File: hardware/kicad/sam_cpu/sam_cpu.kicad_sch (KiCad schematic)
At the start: 0 parts

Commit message: Redraw the schematic with wires (draft 0.2)
Every connection is now a wire, and each connector sits on the page of the
parts that drive or read it (Pi header with the RP2354B, J6/J12 with their
comparators and 74HC165, J1 with the 74HC595, J2/J3/J13 with their filters).
Signals between pages use global labels with page references. The Pi page is
merged into the MCU page; the Pi 4 sits on the 40-pin header J21.

ERC: 0 errors, 1 warning. Netlist check: 1266 pins, 299 nets, no differences.

Co-Authored-By: Claude Opus 5.5 (1M context) <noreply@anthropic.com>
Claude-Session: https://claude.ai/code/session_019DLTv1F2PjepjxqiUcAMKV
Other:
- sheet MCU renamed MCU and Pi
- removed sheet Dedicated switches
- removed sheet Raspberry Pi
- removed sheet Switch returns
- removed sheet Switch scan
- added sheet Dedicated switches 1-16 (sw_dedicated_1.kicad_sch)
- added sheet Dedicated switches 17-24 (sw_dedicated_2.kicad_sch)
- added sheet Switch columns (sw_columns.kicad_sch)
- added sheet Switch rows 1-8 (sw_rows_1.kicad_sch)
- added sheet Switch rows 9-16 (sw_rows_9.kicad_sch)
- sheet Audio ports: added none; removed I2S_BCK, I2S_DIN, I2S_LRCK
- sheet Display and GI ports: added none; removed DMD_COLLATCH_A, DMD_COLLATCH_B, DMD_DE, DMD_PIXCLK, DMD_ROWCLK, DMD_ROWDATA, DMD_SDATA, GI_PWM, GI_SPARE
- sheet IO bus ports: added none; removed BUS_A0, BUS_A1, BUS_A2, BUS_A3, BUS_D0, BUS_D1, BUS_D2, BUS_D3, BUS_D4, BUS_D5, BUS_D6, BUS_D7, BUS_DIR, BUS_IOSTB, BUS_OE_N, NBRESET_DRV
- sheet MCU and Pi ports: added none; removed BOOTSEL, BUS_A0, BUS_A1, BUS_A2, BUS_A3, BUS_D0, BUS_D1, BUS_D2, BUS_D3, BUS_D4, BUS_D5, BUS_D6, BUS_D7, BUS_DIR, BUS_IOSTB, BUS_OE_N, DMD_COLLATCH_A, DMD_COLLATCH_B, DMD_DE, DMD_PIXCLK, DMD_ROWCLK, DMD_ROWDATA, DMD_SDATA, FRAME_CS_N, FRAME_MOSI, FRAME_SCK, GI_PWM, GI_SPARE, MEM_PROTECT, MR_N, NBRESET_DRV, RP_IRQ_N, RP_UART_RX, RP_UART_TX, STB_DATA, STB_LATCH, SWCLK, SWDIO, SW_CLK, SW_DATA, SW_LOAD_N, VMON_12V, VMON_5V
- sheet Power ports: added none; removed VMON_12V, VMON_5V
- note added: "Audio: Pi I2S -> PCM5102A -> 2 x TDA2030A on +-12 V -> J10"
- note added: "Dedicated switches D1-D16 (J2, J3) and coin door memory protect"
- note added: "Dedicated switches D17-D24 (J13) and DIP switches"
- note added: "J5 original DMD driver and J18 GI dimmer header"
- note added: "J9: bus to the IO power driver board (IO board J1)"
- note added: "Power: +5 V mux (external / J11), 3.3 V, 4.5 V, supply monitors"
- note added: "RP2354B SAM IO controller and Raspberry Pi 4 header"
- note added: "SAM CPU replacement board, draft 0.2, drawn from docs/ARCHITECTURE.md. Licence: CERN-OHL-S v2. A Raspberry Pi 4 on the 40-pin header J21 runs PinMAME + ppuc (HDMI stays on the Pi). The RP2354B drives the original IO power driver board on J9 and scans the switches. Connector names and pinouts follow the original CPU/Sound board 520-5246-00. Each connector sits on the same page as the circuit that 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"
- note added: "Switch matrix columns: 74HC595, strobe drivers, J1"
- note added: "Switch matrix returns 1-8: J6, LM339 front end, 74HC165"
- note added: "Switch matrix returns 9-16: J12, LM339 front end, 74HC165"
- note removed: "SAM CPU replacement board, draft 0.1, drawn from docs/ARCHITECTURE.md. A Raspberry Pi 4 / CM4 runs PinMAME + ppuc. The RP2354B drives the original IO power driver board on J9 and scans the switches. Connector names and pinouts follow the original CPU/Sound board 520-5246-00. Licence: CERN-OHL-S v2."

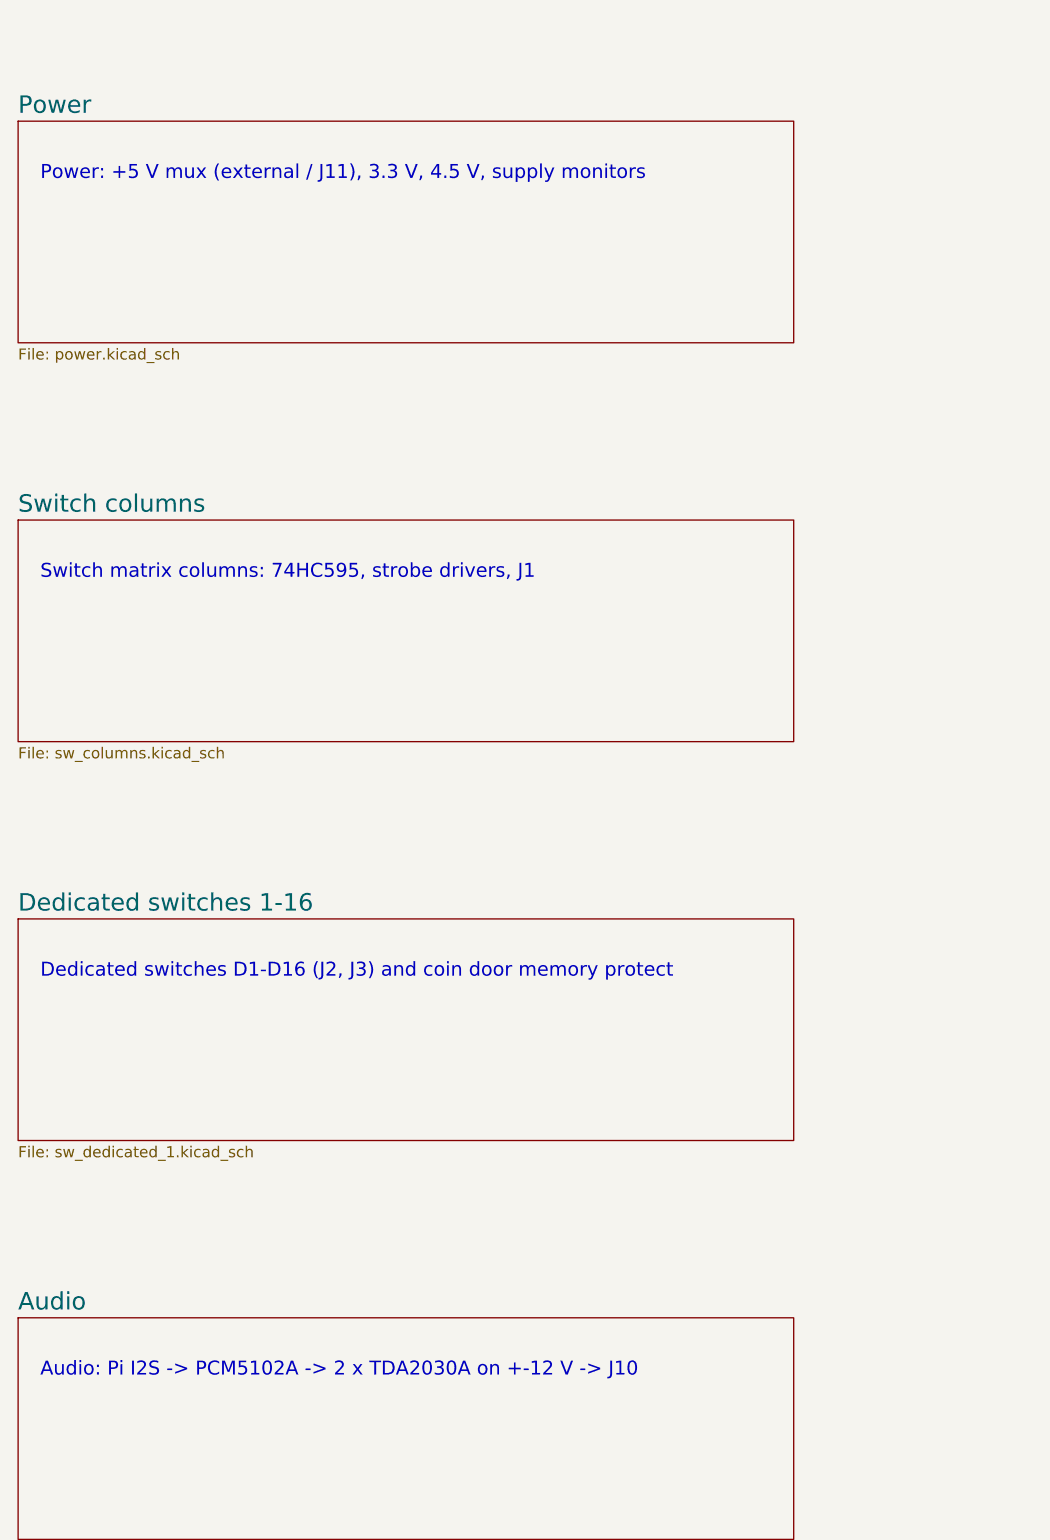
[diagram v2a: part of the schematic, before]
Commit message: Audio on external 12 V with TDA7297 stereo + subwoofer amps, NCP1117, guide regulator layout
- Remove the +-12 V input from J11; J23 external +12 V with polyfuse and TVS
- Replace the two TDA2030A with a TDA7297 bridge amp for left/right (J10, J22)
  and a second TDA7297 for the subwoofer (J24), fed by an (L+R)/2 110 Hz
  Sallen-Key low-pass (OPA1678); shared standby and RP2354B-controlled mute
- AMS1117 -> NCP1117-3.3 (ceramic-stable, as in the RP2350 guide), 10 uF 1206
- L1 and crystal part numbers from the RP2350 hardware guide
- Place the core regulator parts by hand following the Pico 2 layout; amps in a
  row with a heatsink keep-out; J23/J22/J24 on the right edge

Co-Authored-By: Claude Opus 5.5 (1M context) <noreply@anthropic.com>
Claude-Session: https://claude.ai/code/session_01ExuDVoDDDHhVWjb8EwVzYb
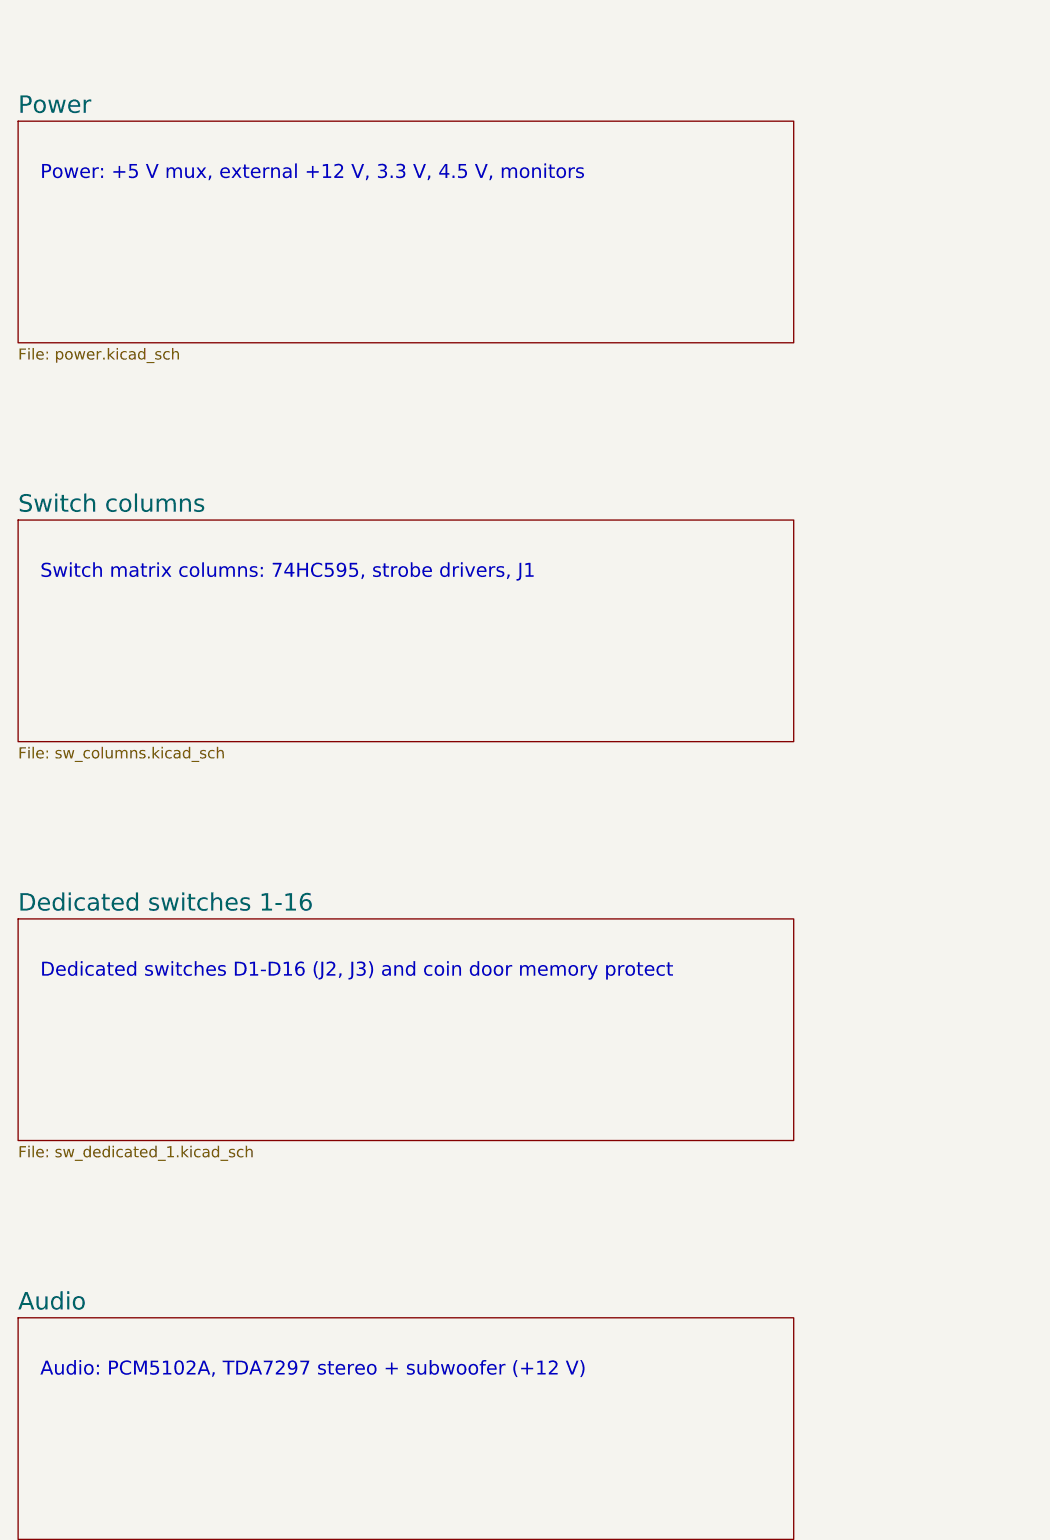
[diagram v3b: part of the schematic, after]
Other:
- note added: "Audio: PCM5102A, TDA7297 stereo + subwoofer (+12 V)"
- note added: "Power: +5 V mux, external +12 V, 3.3 V, 4.5 V, monitors"
- note removed: "Audio: Pi I2S -> PCM5102A -> 2 x TDA2030A on +-12 V -> J10"
- note removed: "Power: +5 V mux (external / J11), 3.3 V, 4.5 V, supply monitors"
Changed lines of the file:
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@@
 		)
 	)
-	(text "Power: +5 V mux (external / J11), 3.3 V, 4.5 V, supply monitors"
+	(text "Power: +5 V mux, external +12 V, 3.3 V, 4.5 V, monitors"
 		(exclude_from_sim no)
 		(at 27.94 68.58 0)
@@
 		)
 	)
-	(text "Audio: Pi I2S -> PCM5102A -> 2 x TDA2030A on +-12 V -> J10"
+	(text "Audio: PCM5102A, TDA7297 stereo + subwoofer (+12 V)"
 		(exclude_from_sim no)
 		(at 27.94 205.74 0)

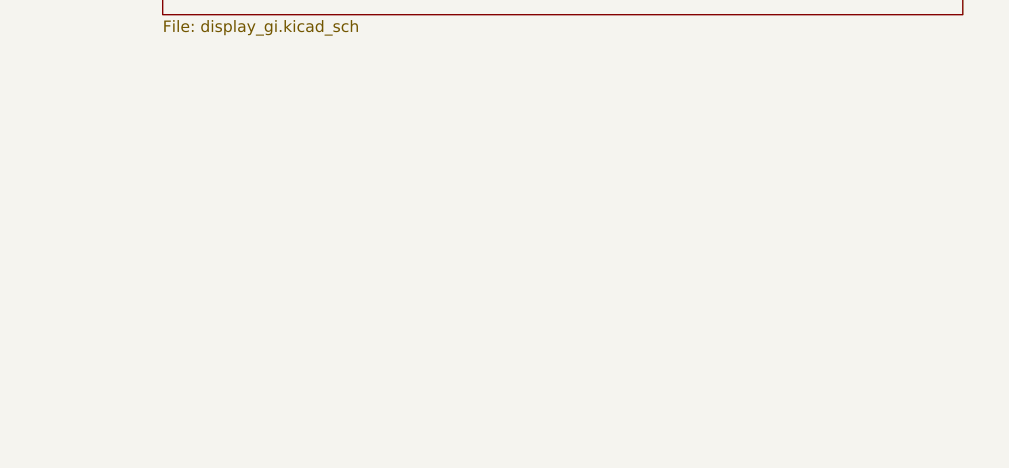
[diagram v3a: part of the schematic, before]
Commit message: Add two HD DMD panels on a PIO parallel bus (incremental edit)
RP2354B GPIO20-36 drive two HUB75 panels (J25/J26) through 3 x 74AHCT245
with shared CLK/LAT/OE and A/B row lines; J5 shares DMD_D0-D6. The 165
load and 595 latch share GPIO17; coin door moves to a 7th 165 (U30),
LED_STATUS and GI_SPARE to a new first 595 (U31). Board widened to 142 mm
below the Pi. Sheets and board edited in place via tools/changes, no
existing footprint moved.

Co-Authored-By: Claude Opus 5.5 (1M context) <noreply@anthropic.com>
Claude-Session: https://claude.ai/code/session_01ExuDVoDDDHhVWjb8EwVzYb
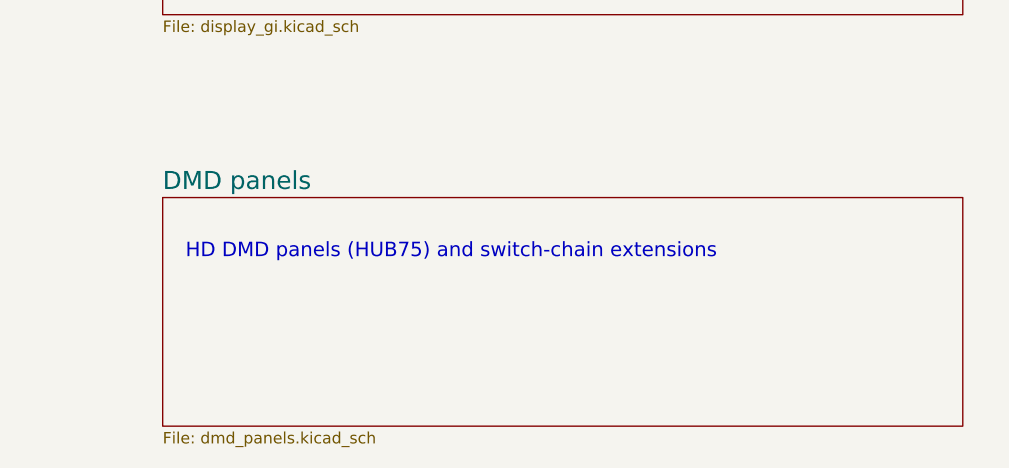
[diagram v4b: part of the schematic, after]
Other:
- added sheet DMD panels (dmd_panels.kicad_sch)
- note added: "HD DMD panels (HUB75) and switch-chain extensions"
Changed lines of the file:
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@@
+		)
+	)
+	(sheet
+		(at 279.4 200.66)
+		(size 88.9 25.4)
+		(exclude_from_sim no)
+		(in_bom yes)
+		(on_board yes)
+		(dnp no)
+		(fields_autoplaced yes)
+		(stroke
+			(width 0.1524)
+			(type solid)
+		)
+		(fill
+			(color 0 0 0 0)
+		)
+		(property "Sheetname" "DMD panels"
+			(at 279.4 199.9484 0)
+			(show_name no)
+			(do_not_autoplace no)
+			(effects
+				(font
+					(size 2 2)
+				)
+				(justify left bottom)
+			)
+		)
+		(property "Sheetfile" "dmd_panels.kicad_sch"
+			(at 279.4 226.6484 0)
+			(show_name no)
+			(do_not_autoplace no)
+			(effects
+				(font
+					(size 1.27 1.27)
+				)
+				(justify left top)
+			)
+		)
+		(instances
+			(project "sam_cpu"
+				(path "/2aea4fdf-a573-57d0-a5af-7bd6ce737647"
+					(page "12")
+				)
+			)
+		)
+	)
+	(text "HD DMD panels (HUB75) and switch-chain extensions"
+		(exclude_from_sim no)
+		(at 281.94 205.74 0)
+		(effects
+			(font
+				(size 1.6 1.6)
+			)
+			(justify left top)
 		)
 	)

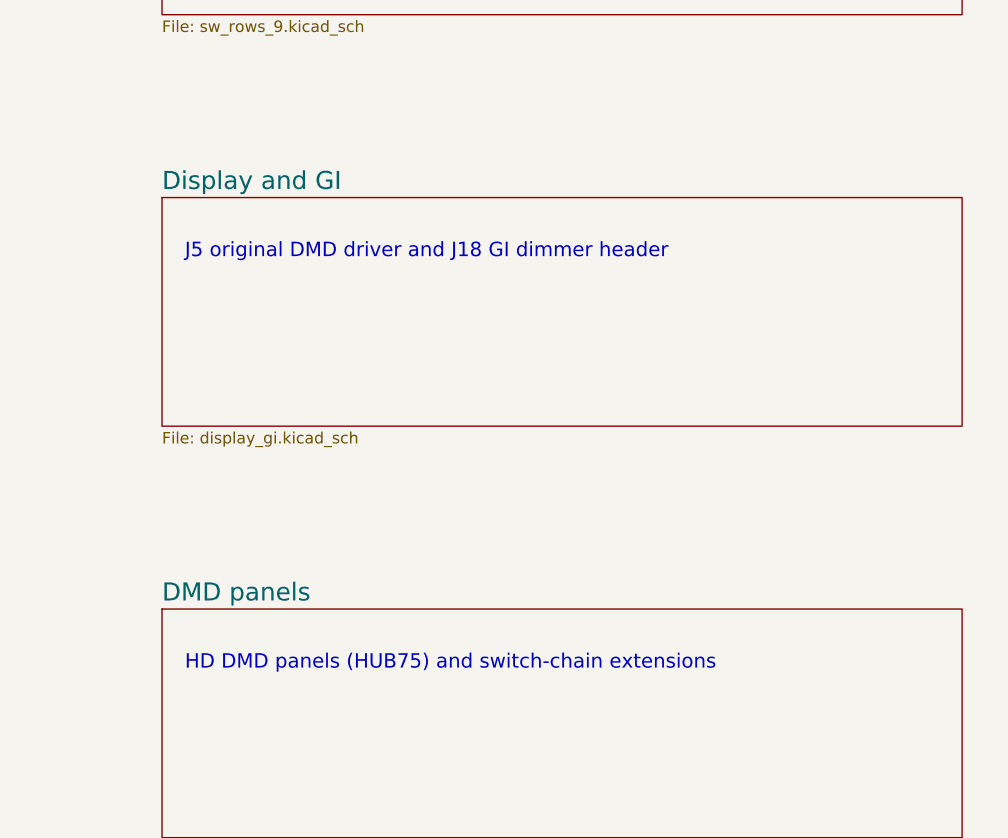
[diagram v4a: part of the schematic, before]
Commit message: Remove both DMD interfaces from the schematic and the board
DMD signals do not survive the long cabinet wires (Vincent, 2026-10-07).
Removed: J5 original DMD driver (U21, RN4, RN5, R176-R182, C95) and the
HD panel bus (J25, J26, U27-U29, RN6-RN11, C122-C124, TP23, TP24), their
tracks and fan-out vias. U30 / U31 stay (switch chain). RP2354B GPIO20-36
are unassigned (no-connect flags). The board goes back to the original
120.65 x 231.76 mm outline. DRC: 20 connections still open (was 35).

Co-Authored-By: Claude Opus 5.5 (1M context) <noreply@anthropic.com>
Claude-Session: https://claude.ai/code/session_01ExuDVoDDDHhVWjb8EwVzYb
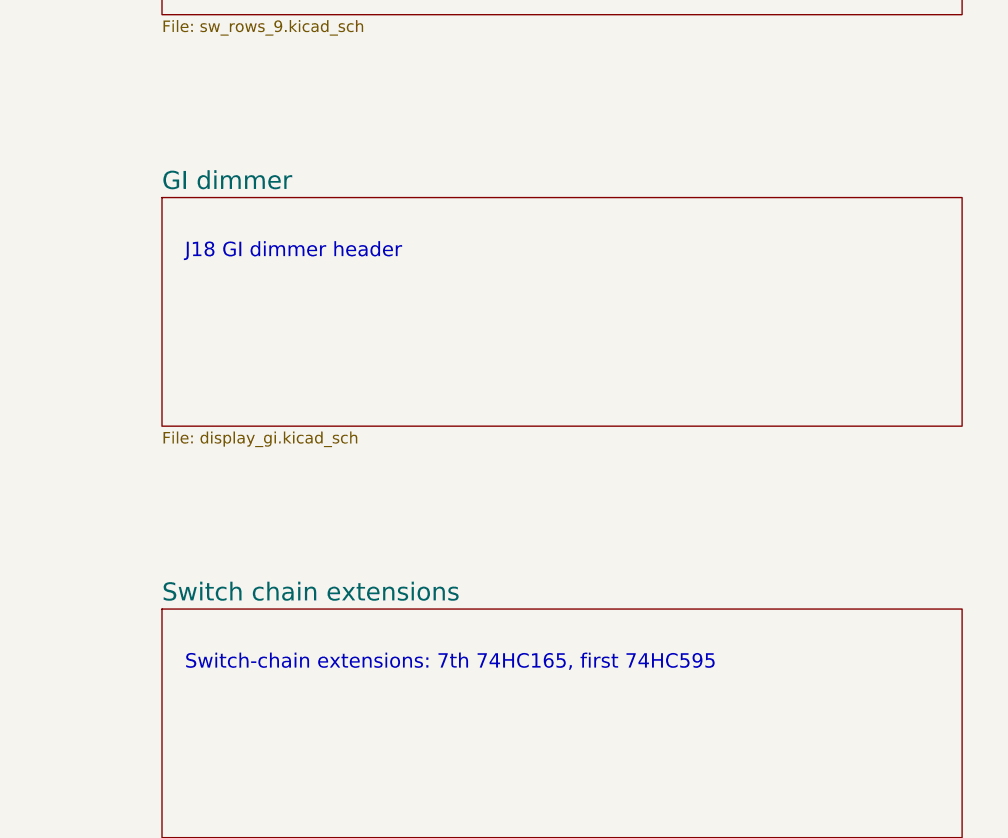
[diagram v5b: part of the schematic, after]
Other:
- sheet DMD panels renamed Switch chain extensions
- sheet Display and GI renamed GI dimmer
- note added: "J18 GI dimmer header"
- note added: "Switch-chain extensions: 7th 74HC165, first 74HC595"
- note removed: "HD DMD panels (HUB75) and switch-chain extensions"
- note removed: "J5 original DMD driver and J18 GI dimmer header"
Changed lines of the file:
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@@
 		)
 	)
-	(text "J5 original DMD driver and J18 GI dimmer header"
+	(text "J18 GI dimmer header"
 		(exclude_from_sim no)
 		(at 281.94 160.02 0)
@@
 			(color 0 0 0 0)
 		)
-		(property "Sheetname" "DMD panels"
+		(property "Sheetname" "Switch chain extensions"
 			(at 279.4 199.9484 0)
 			(show_name no)
@@
 		)
 	)
-	(text "HD DMD panels (HUB75) and switch-chain extensions"
+	(text "Switch-chain extensions: 7th 74HC165, first 74HC595"
 		(exclude_from_sim no)
 		(at 281.94 205.74 0)
@@
 			(color 0 0 0 0)
 		)
-		(property "Sheetname" "Display and GI"
+		(property "Sheetname" "GI dimmer"
 			(at 279.4 154.2284 0)
 			(show_name no)
